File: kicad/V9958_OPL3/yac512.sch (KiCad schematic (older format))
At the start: 9 parts, among them P1 CONN_01X02, P2 CONN_01X02, U10 RC4136, U9 YAC512

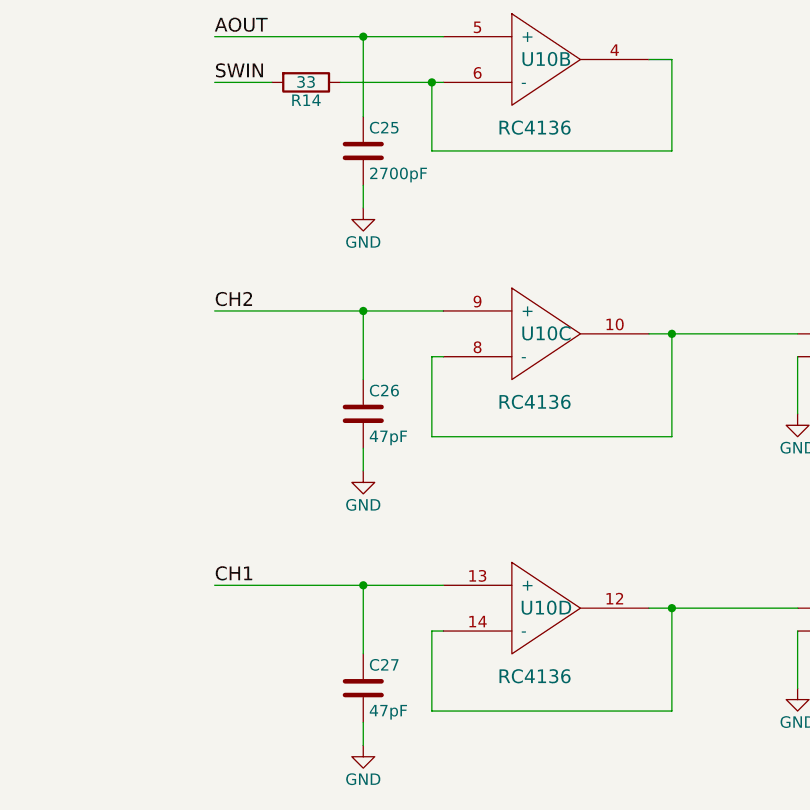
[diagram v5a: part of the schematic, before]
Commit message: capacitor values fixed
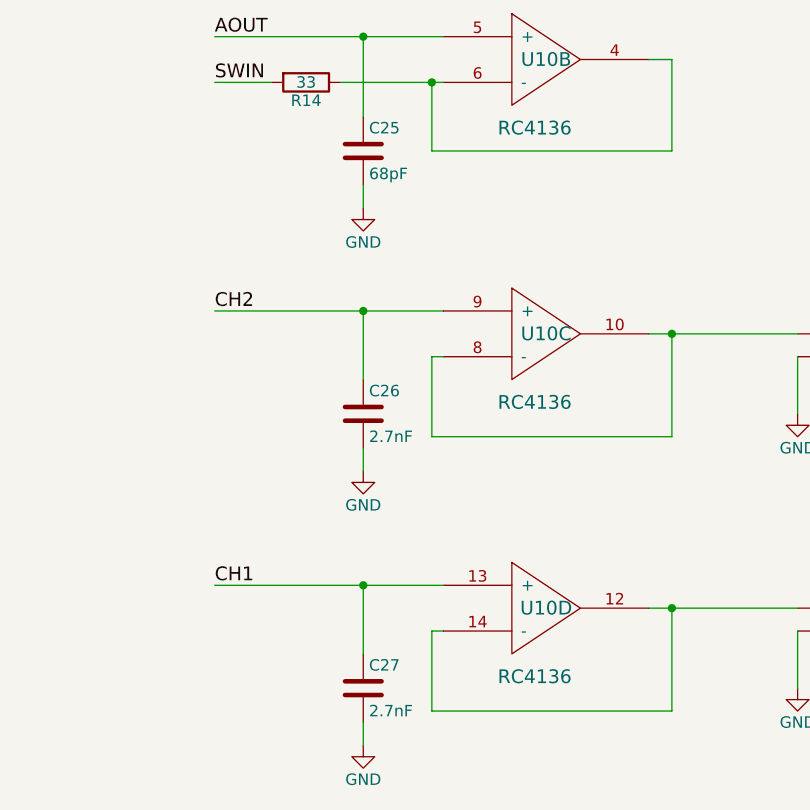
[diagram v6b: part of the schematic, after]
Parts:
- C25: value 2700pF -> 68pF
- C26, C27: value 47pF -> 2.7nF
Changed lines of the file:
@@
 P 7300 2800
 F 0 "C25" H 7325 2900 50  0000 L CNN
-F 1 "2700pF" H 7325 2700 50  0000 L CNN
+F 1 "68pF" H 7325 2700 50  0000 L CNN
 F 2 "Capacitors_ThroughHole:C_Disc_D3_P2.5" H 7338 2650 50  0001 C CNN
 F 3 "" H 7300 2800 50  0000 C CNN
@@
 P 7300 3950
 F 0 "C26" H 7325 4050 50  0000 L CNN
-F 1 "47pF" H 7325 3850 50  0000 L CNN
+F 1 "2.7nF" H 7325 3850 50  0000 L CNN
 F 2 "Capacitors_ThroughHole:C_Disc_D3_P2.5" H 7338 3800 50  0001 C CNN
 F 3 "" H 7300 3950 50  0000 C CNN
@@
 P 7300 5150
 F 0 "C27" H 7325 5250 50  0000 L CNN
-F 1 "47pF" H 7325 5050 50  0000 L CNN
+F 1 "2.7nF" H 7325 5050 50  0000 L CNN
 F 2 "Capacitors_ThroughHole:C_Disc_D3_P2.5" H 7338 5000 50  0001 C CNN
 F 3 "" H 7300 5150 50  0000 C CNN
